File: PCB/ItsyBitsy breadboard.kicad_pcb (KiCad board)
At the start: 2 copper layers, 63.5 x 22.9 mm, 26 parts, among them J1 EDGE PINS, J2 EDGE PINS, J4 STEMMA, J5 BATTERY, J6 XTRA, J7 BODGE PINS, J8 EDGE PINS, Q1 BSS138DW-7-F, U1 MCP73831-2-OT

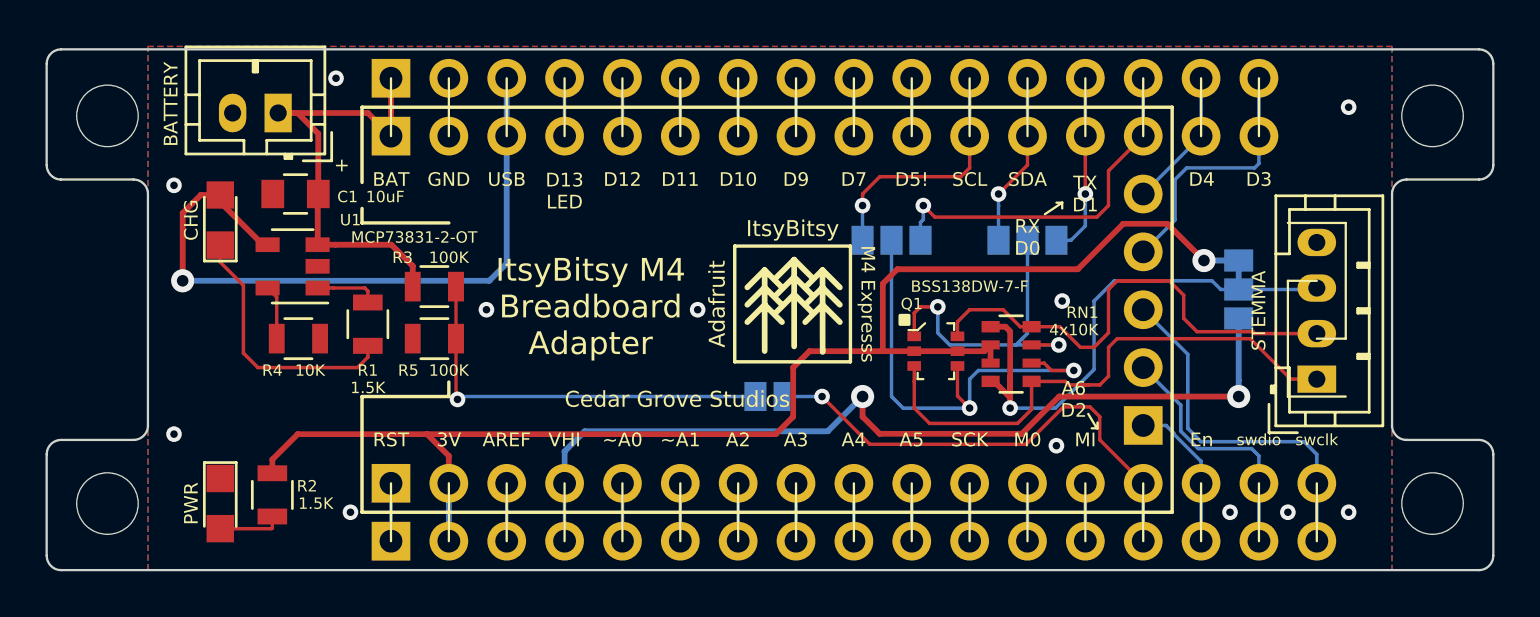
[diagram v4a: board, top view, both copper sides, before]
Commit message: add default Stemma jumpers
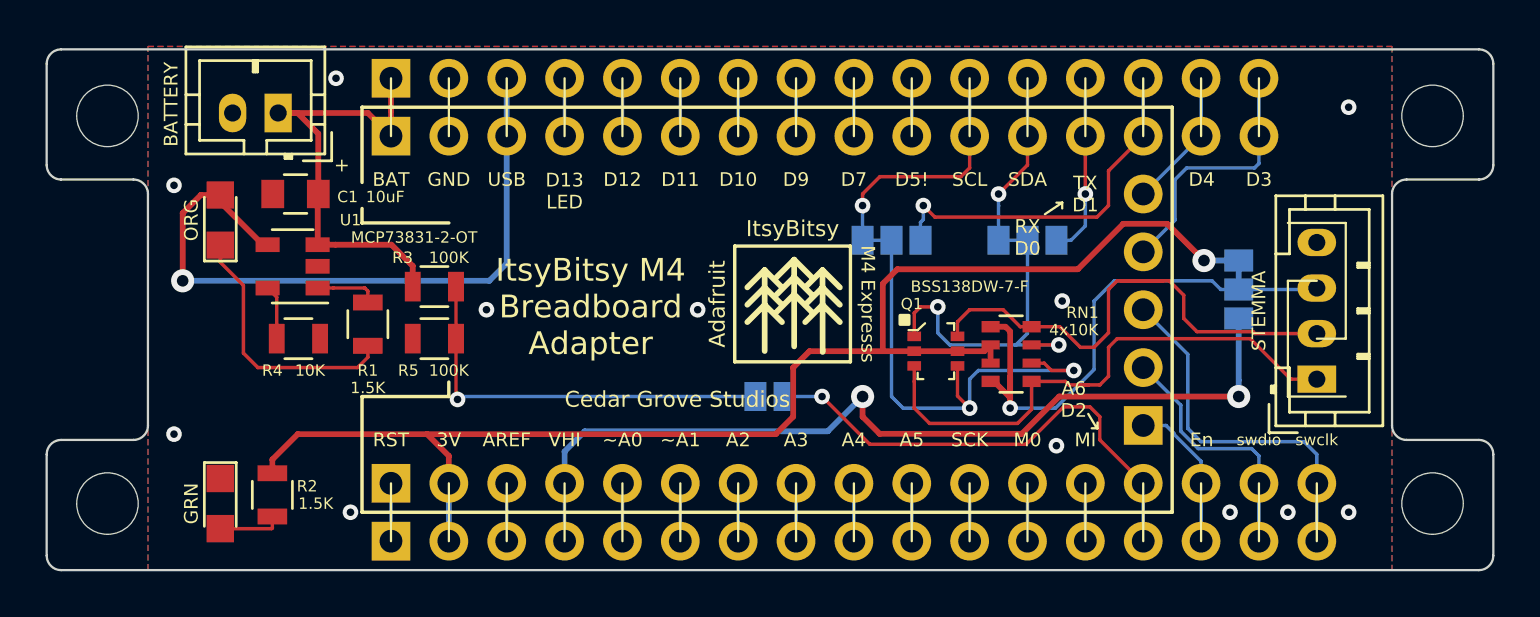
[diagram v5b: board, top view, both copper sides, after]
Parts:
- D1: value CHG -> ORG
- D2: value PWR -> GRN
- JMP3: value Vbat -> A6 -> Vbat
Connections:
- JMP1 pad 2: /SCL_RX -> /SCL
- JMP2 pad 2: /SDA_TX -> /SDA
- Q1 pad 1: /SDA_TX -> /SDA
- Q1 pad 4: /SCL_RX -> /SCL
- RN1 pad 6: /SCL_RX -> /SCL
- RN1 pad 7: /SDA_TX -> /SDA
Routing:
- net /SCL: track 11.1 -> 33.0 mm, vias 1 -> 3
- net /SCL_RX: track 20.6 -> 0.00 mm, vias 2 -> 0
- net /SDA: track 7.64 -> 23.8 mm, vias 1 -> 3
- net /SDA_TX: track 14.8 -> 0.00 mm, vias 2 -> 0

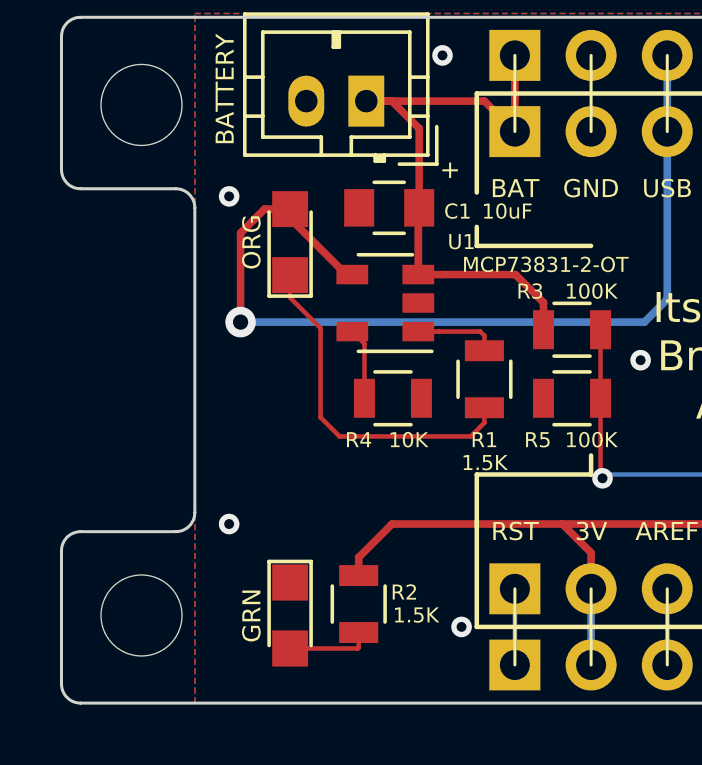
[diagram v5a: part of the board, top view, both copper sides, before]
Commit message: update PCB silkscreen
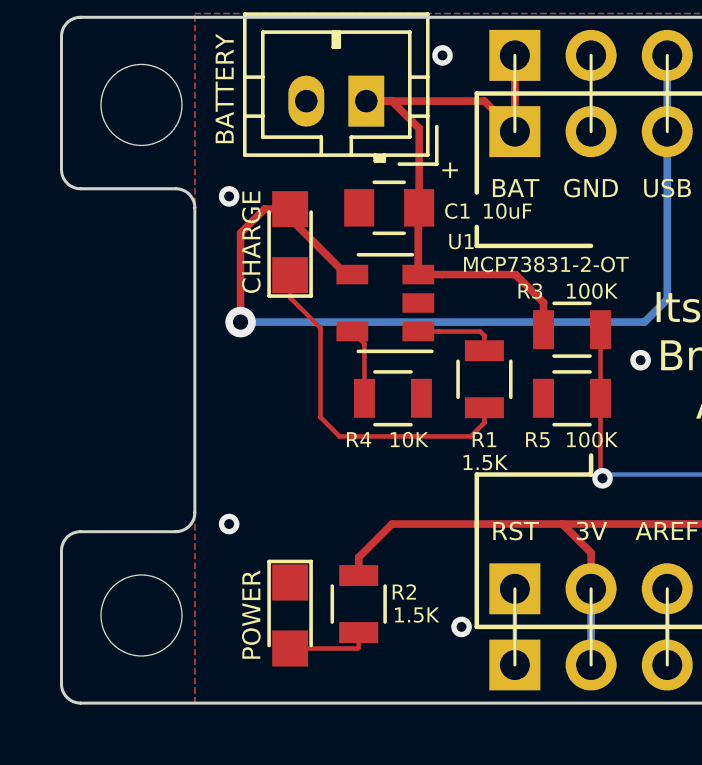
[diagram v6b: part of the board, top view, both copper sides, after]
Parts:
- D1: value ORG -> CHARGE
- D2: value GRN -> POWER
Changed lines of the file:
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@@
     )
     (model "C:/Program Files/KiCad/share/kicad/packages3d/Pin_Headers.3dshapes/Pin_Header_Straight_1x05_Pitch2.54mm.wrl"
-      (offset (xyz 0 -5.08 17.9))
+      (offset (xyz 0 -5.08 6.9))
       (scale (xyz 1 1 0.6))
       (rotate (xyz 0 180 90))
     )
     (model "C:/Program Files/KiCad/share/kicad/packages3d/Pin_Headers.3dshapes/Pin_Header_Straight_1x14_Pitch2.54mm.wrl"
-      (offset (xyz 16.51 -12.7 17.9))
+      (offset (xyz 16.51 -12.7 6.9))
       (scale (xyz 1 1 0.6))
       (rotate (xyz 0 180 0))
     )
     (model "C:/Program Files/KiCad/share/kicad/packages3d/Pin_Headers.3dshapes/Pin_Header_Straight_1x14_Pitch2.54mm.wrl"
-      (offset (xyz 16.51 2.54 17.9))
+      (offset (xyz 16.51 2.54 6.9))
       (scale (xyz 1 1 0.6))
       (rotate (xyz 0 180 0))
     )
     (model "C:/Program Files/KiCad/share/kicad/packages3d/Adafruit_CAD_Parts-master/3800 ItsyBitsy M4/3800-ItsyBitsy-M4.step"
-      (offset (xyz 34.25 4 18))
+      (offset (xyz 34.25 4 7))
       (scale (xyz 1 1 1))
       (rotate (xyz 0 0 180))
@@
       (effects (font (size 0.5 0.5) (thickness 0.1)))
     )
-    (fp_text value ORG (at 0 -1.27 90) (layer F.SilkS)
+    (fp_text value CHARGE (at 0 -1.27 90) (layer F.SilkS)
       (effects (font (size 0.6 0.6) (thickness 0.12)))
     )
@@
       (effects (font (size 0.5 0.5) (thickness 0.1)))
     )
-    (fp_text value GRN (at 0 1.27 270) (layer F.SilkS)
+    (fp_text value POWER (at 0 1.27 270) (layer F.SilkS)
       (effects (font (size 0.6 0.6) (thickness 0.12)))
     )
